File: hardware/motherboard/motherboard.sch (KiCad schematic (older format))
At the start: 74 parts, among them J1 Conn_01x04_Female, J10 Conn_01x02_Female, J11 Conn_01x02_Female, J12 Conn_01x03_Male, J13 Conn_01x03_Male, J14 Conn_01x03_Male, J15 Conn_01x06_Female, J2 Conn_01x03_Male, J3 Conn_01x05_Female, J4 Conn_01x05_Female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

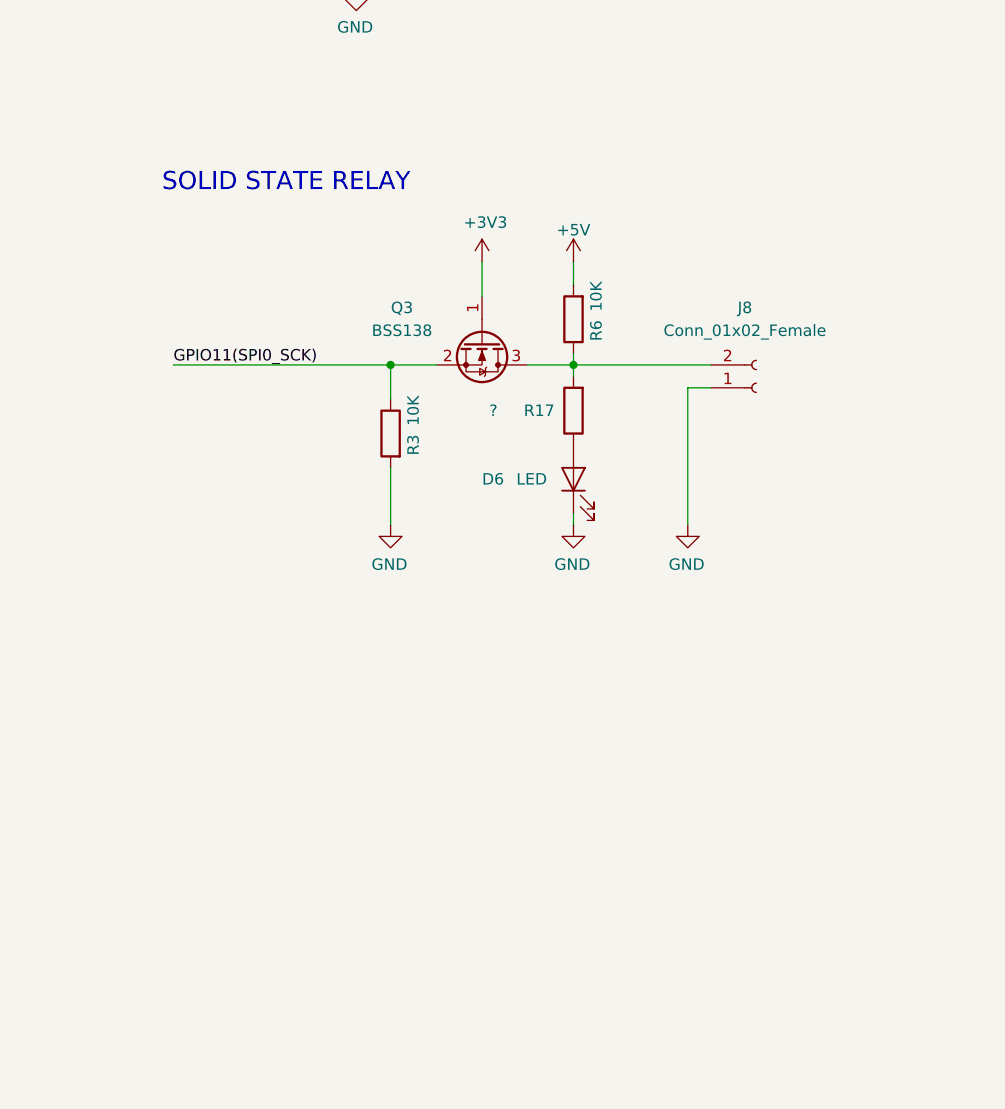
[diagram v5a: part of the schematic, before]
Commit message: exposed another GPIO
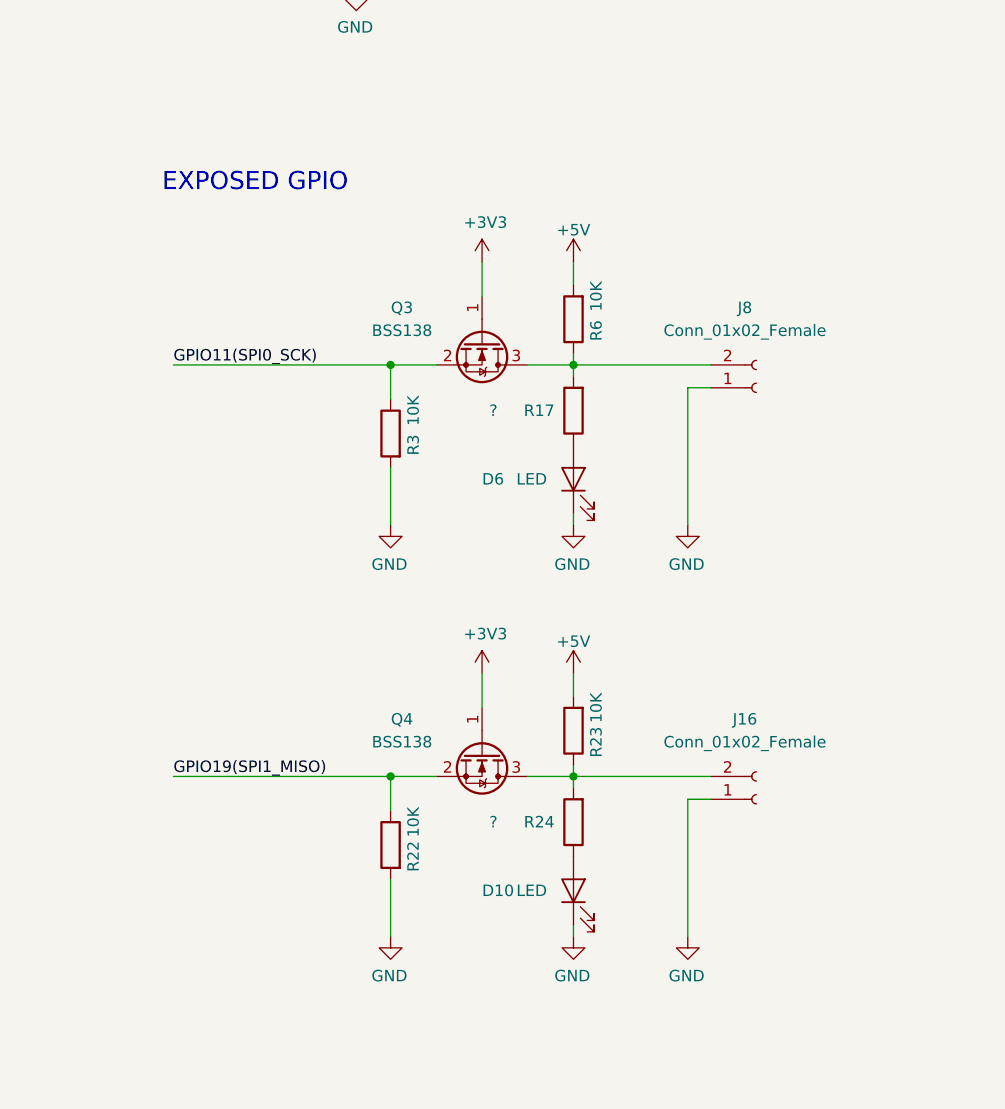
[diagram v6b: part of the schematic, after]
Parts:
- added D10: LED, LED_SMD:LED_1210_3225Metric_Pad1.42x2.65mm_HandSolder, symbol Device:LED
- added J16: Conn_01x02_Female, TerminalBlock:TerminalBlock_bornier-2_P5.08mm, symbol Connector:Conn_01x02_Female
- added Q4: BSS138, Package_TO_SOT_SMD:SOT-23_Handsoldering, symbol Transistor_FET:BSS138
- added R22, R23: 10K, Resistor_SMD:R_1210_3225Metric_Pad1.42x2.65mm_HandSolder, symbol Device:R
- added R24: ?, Resistor_SMD:R_1210_3225Metric_Pad1.42x2.65mm_HandSolder, symbol Device:R
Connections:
- net +3V3: now also Q4.1 (G)
- net +5V: now also R23.2
- net GND: now also D10.1 (K), J16.1 (Pin_1), R22.2
- net GPIO19(SPI1_MISO): now also Q4.2 (S), R22.1
- new net: J16.2 (Pin_2), Q4.3 (D), R23.1, R24.2
- new net: D10.2 (A), R24.1
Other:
- note added: "EXPOSED GPIO"
- note removed: "SOLID STATE RELAY"
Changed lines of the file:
@@
 Connection ~ 7050 3700
 Text Notes 4700 5700 0    79   ~ 0
-SOLID STATE RELAY
+EXPOSED GPIO
 Connection ~ 6950 2000
 Wire Wire Line
@@
 $EndComp
 $Comp
-L power:+12V #PWR?
+L power:+12V #PWR0127
 U 1 1 60087395
 P 10250 5550
-F 0 "#PWR?" H 10250 5400 50  0001 C CNN
+F 0 "#PWR0127" H 10250 5400 50  0001 C CNN
 F 1 "+12V" H 10265 5723 50  0000 C CNN
 F 2 "" H 10250 5550 50  0001 C CNN
@@
 Wire Wire Line
 	10250 6650 10250 5550
+$Comp
+L power:GND #PWR0128
+U 1 1 5FA5EFA9
+P 7000 8950
+F 0 "#PWR0128" H 7000 8700 50  0001 C CNN
+F 1 "GND" H 7005 8777 50  0000 C CNN
+F 2 "" H 7000 8950 50  0001 C CNN
+F 3 "" H 7000 8950 50  0001 C CNN
+	1    7000 8950
+	-1   0    0    -1
+$EndComp
+$Comp
+L Connector:Conn_01x02_Female J16
+U 1 1 5FA5EFAF
+P 7300 8350
+F 0 "J16" H 7250 8000 50  0000 C CNN
+F 1 "Conn_01x02_Female" H 7250 8100 50  0000 C CNN
+F 2 "TerminalBlock:TerminalBlock_bornier-2_P5.08mm" H 7300 8350 50  0001 C CNN
+F 3 "~" H 7300 8350 50  0001 C CNN
+	1    7300 8350
+	1    0    0    1
+$EndComp
+Wire Wire Line
+	6300 8250 6500 8250
+$Comp
+L Transistor_FET:BSS138 Q4
+U 1 1 5FA5EFB7
+P 6100 8150
+F 0 "Q4" V 5950 7800 50  0000 C CNN
+F 1 "BSS138" V 6050 7800 50  0000 C CNN
+F 2 "Package_TO_SOT_SMD:SOT-23_Handsoldering" H 6300 8075 50  0001 L CIN
+F 3 "https://www.fairchildsemi.com/datasheets/BS/BSS138.pdf" H 6100 8150 50  0001 L CNN
+	1    6100 8150
+	0    1    1    0
+$EndComp
+$Comp
+L Device:R R22
+U 1 1 5FA5EFBD
+P 5700 8550
+F 0 "R22" V 5600 8500 50  0000 C CNN
+F 1 "10K" V 5600 8650 50  0000 C CNN
+F 2 "Resistor_SMD:R_1210_3225Metric_Pad1.42x2.65mm_HandSolder" V 5630 8550 50  0001 C CNN
+F 3 "~" H 5700 8550 50  0001 C CNN
+	1    5700 8550
+	-1   0    0    -1
+$EndComp
+$Comp
+L power:+5V #PWR0132
+U 1 1 5FA5EFC3
+P 6500 7800
+F 0 "#PWR0132" H 6500 7650 50  0001 C CNN
+F 1 "+5V" H 6500 7940 50  0000 C CNN
+F 2 "" H 6500 7800 50  0000 C CNN
+F 3 "" H 6500 7800 50  0000 C CNN
+	1    6500 7800
+	1    0    0    -1
+$EndComp
+$Comp
+L power:+3V3 #PWR0133
+U 1 1 5FA5EFC9
+P 6100 7800
+F 0 "#PWR0133" H 6100 7650 50  0001 C CNN
+F 1 "+3V3" H 6115 7973 50  0000 C CNN
+F 2 "" H 6100 7800 50  0001 C CNN
+F 3 "" H 6100 7800 50  0001 C CNN
+	1    6100 7800
+	1    0    0    -1
+$EndComp
+Connection ~ 6500 8250
+Wire Wire Line
+	7000 8950 7000 8350
+Wire Wire Line
+	7000 8350 7100 8350
+$Comp
+L Device:R R24
+U 1 1 5FA5EFD2
+P 6500 8450
+F 0 "R24" H 6650 8450 50  0000 C CNN
+F 1 "?" H 6850 8450 50  0000 C CNN
+F 2 "Resistor_SMD:R_1210_3225Metric_Pad1.42x2.65mm_HandSolder" V 6430 8450 50  0001 C CNN
+F 3 "~" H 6500 8450 50  0001 C CNN
+	1    6500 8450
+	-1   0    0    1
+$EndComp
+$Comp
+L Device:LED D10
+U 1 1 5FA5EFD8
+P 6500 8750
+F 0 "D10" V 6500 9150 50  0000 R CNN
+F 1 "LED" V 6500 9000 50  0000 R CNN
+F 2 "LED_SMD:LED_1210_3225Metric_Pad1.42x2.65mm_HandSolder" H 6500 8750 50  0001 C CNN
+F 3 "~" H 6500 8750 50  0001 C CNN
+	1    6500 8750
+	0    -1   -1   0
+$EndComp
+Wire Wire Line
+	6500 8300 6500 8250
+$Comp
+L power:GND #PWR0134
+U 1 1 5FA5EFDF
+P 6500 8950
+F 0 "#PWR0134" H 6500 8700 50  0001 C CNN
+F 1 "GND" H 6505 8777 50  0000 C CNN
+F 2 "" H 6500 8950 50  0001 C CNN
+F 3 "" H 6500 8950 50  0001 C CNN
+	1    6500 8950
+	-1   0    0    -1
+$EndComp
+Wire Wire Line
+	6500 8950 6500 8900
+Wire Wire Line
+	7100 8250 6500 8250
+Wire Wire Line
+	4750 8250 5700 8250
+Wire Wire Line
+	6100 7800 6100 7950
+$Comp
+L power:GND #PWR0135
+U 1 1 5FA5EFE9
+P 5700 8950
+F 0 "#PWR0135" H 5700 8700 50  0001 C CNN
+F 1 "GND" H 5705 8777 50  0000 C CNN
+F 2 "" H 5700 8950 50  0001 C CNN
+F 3 "" H 5700 8950 50  0001 C CNN
+	1    5700 8950
+	-1   0    0    -1
+$EndComp
+Wire Wire Line
+	5700 8950 5700 8700
+Wire Wire Line
+	5700 8400 5700 8250
+Connection ~ 5700 8250
+Wire Wire Line
+	5700 8250 5900 8250
+Wire Wire Line
+	6500 7800 6500 7900
+Wire Wire Line
+	6500 8250 6500 8200
+$Comp
+L Device:R R23
+U 1 1 5FA5EFF5
+P 6500 8050
+F 0 "R23" V 6400 8100 50  0000 C CNN
+F 1 "10K" V 6400 7950 50  0000 C CNN
+F 2 "Resistor_SMD:R_1210_3225Metric_Pad1.42x2.65mm_HandSolder" V 6430 8050 50  0001 C CNN
+F 3 "~" H 6500 8050 50  0001 C CNN
+	1    6500 8050
+	-1   0    0    1
+$EndComp
+Text Label 4750 8250 0    50   ~ 0
+GPIO19(SPI1_MISO)
 $EndSCHEMATC

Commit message: version v0.3
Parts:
- removed D10: LED, LED_SMD:LED_1210_3225Metric_Pad1.42x2.65mm_HandSolder, symbol Device:LED
- added J17: Conn_01x03_Male, Connector_PinHeader_2.54mm:PinHeader_1x03_P2.54mm_Vertical, symbol Connector:Conn_01x03_Male
- added J18, J19: Conn_01x01_Female, Connector_Wire:SolderWirePad_1x01_Drill2.5mm, symbol Connector:Conn_01x01_Female
- added Q5: BSS138, Package_TO_SOT_SMD:SOT-23_Handsoldering, symbol Transistor_FET:BSS138
- added R25: ?, Resistor_SMD:R_1210_3225Metric_Pad1.42x2.65mm_HandSolder, symbol Device:R
- R17, R5: value ? -> 10K
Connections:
- net +12V: now also J19.1 (Pin_1); no longer K2.3
- net +3V3: now also J3.4 (Pin_4), R17.1, R2.2, Q5.1 (G); no longer J3.5 (Pin_5), R1.2
- net +5V: now also J3.5 (Pin_5), J7.2 (Pin_2), R1.2, R5.2, J17.3 (Pin_3); no longer J3.4 (Pin_4), J5.3 (Pin_3), J7.5 (Pin_5), R2.2
- net GND: now also R20.1, J17.1 (Pin_1); no longer D8.1 (K)
- net GPIO11(SPI0_SCK): now also R21.2
- net GPIO12(PWM0): now also R25.2
- net GPIO13(PWM1): now also R24.2; no longer R18.2
- net GPIO14(TXD0): no longer R5.2
- net GPIO16: now also R17.2, Q5.2 (S)
- net GPIO19(SPI1_MISO): now also R18.2
- net M1_HA: now also J7.3 (Pin_3); no longer J7.2 (Pin_2)
- net M2_HA: now also J7.4 (Pin_4); no longer J7.3 (Pin_3)
- net M3_HA: now also J7.5 (Pin_5); no longer J7.4 (Pin_4)
- net at J4.1 (Pin_1), K2.1: now also D8.2 (A); no longer R20.2
- net at J5.2 (Pin_2), Q1.3 (D), R16.1: no longer R21.2
- net at J5.4 (Pin_4): now also R5.1, Q5.3 (D)
- net at J5.5 (Pin_5): now also D1.2 (A), K2.2, Q2.3 (D)
- net at J16.2 (Pin_2), Q4.3 (D), R23.1: no longer R24.2
- net at R24.1: now also D6.2 (A)
- net at J8.2 (Pin_2), Q3.3 (D), R6.1: no longer R17.2
- net at R21.1: now also D5.2 (A); no longer D9.2 (A)
- new net: J17.2 (Pin_2), J5.3 (Pin_3)
- new net: J18.1 (Pin_1), K2.3
- new net: D9.2 (A), R25.1
- new net: D8.1 (K), R20.2
- no-connect marks 11 -> 9
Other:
- note added: "5V"
- note added: "EL"
- note added: "GND"
- note added: "Signal"
- note added: "VR"
- note added: "Z/F"
- moved on the sheet: D1, D7, D8, J16, J2, J6, J7, J8, J9, K2, Q1, R16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
